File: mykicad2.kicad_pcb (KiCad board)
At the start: 2 copper layers, 11 parts, among them P1 CONN_01X06, Q1 MMBT3904, Q2 MMBT3906, Q3 IRF9540N

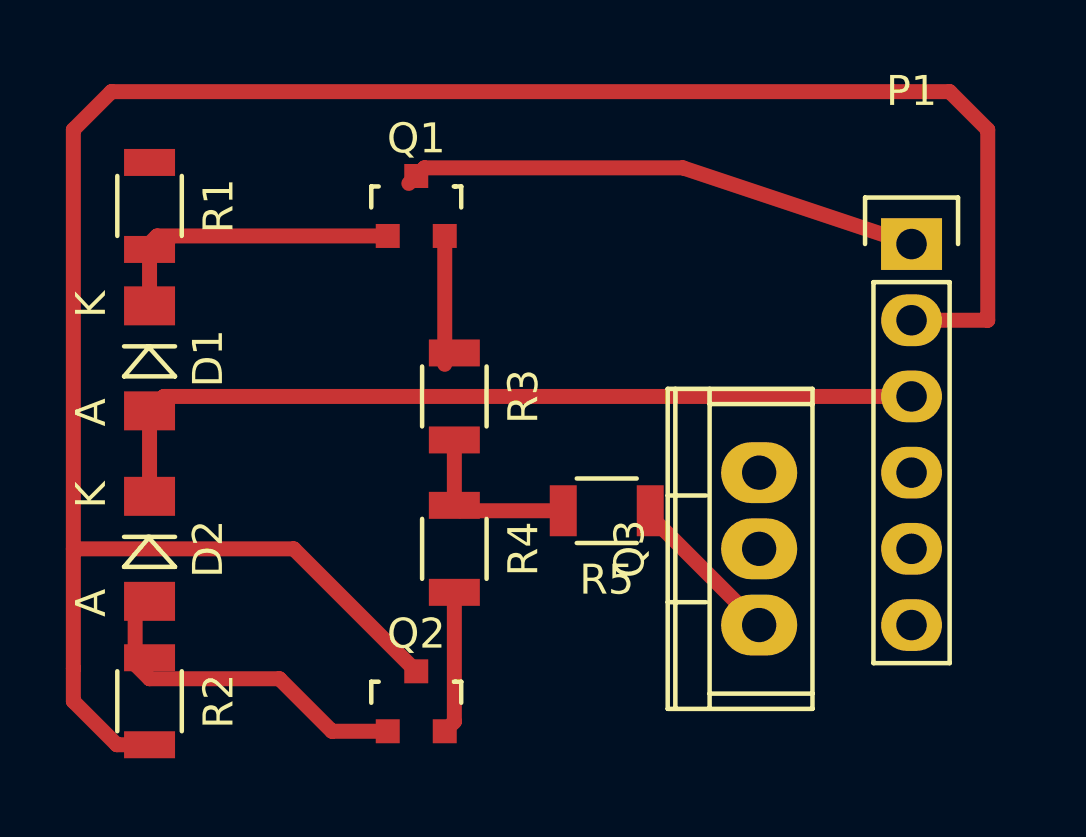
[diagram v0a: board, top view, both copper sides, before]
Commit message: add mosfet update traces
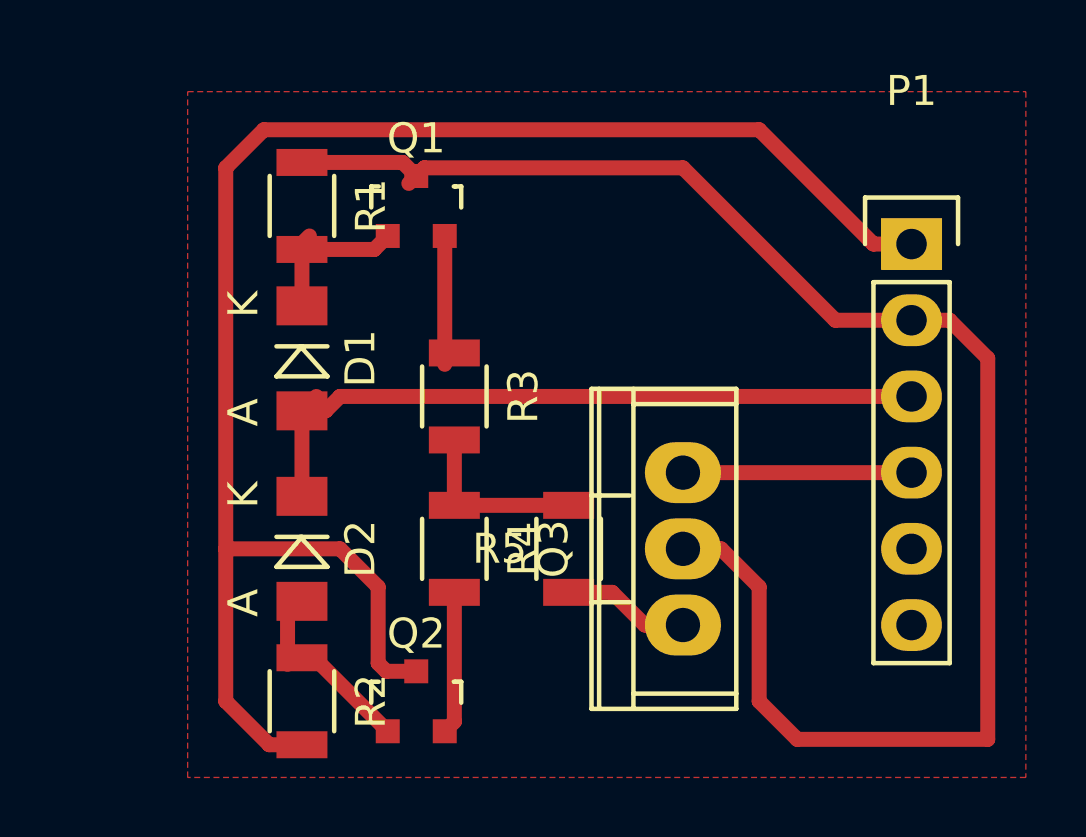
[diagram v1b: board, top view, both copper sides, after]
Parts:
- moved D1 5.08 mm to (154.9, 101.6)
- moved D2 5.08 mm to (154.9, 108.0)
- moved R1 5.08 mm to (154.9, 96.5)
- moved R2 5.08 mm to (154.9, 113.0)
- moved Q3 2.54 mm to (167.6, 108.0)
- moved R5 1.80 mm to (163.8, 108.0), turned to 90 degrees
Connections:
- P1 pad 1: VDD -> GND
- P1 pad 2: GND -> VDD
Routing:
- net VDD: track 17.4 -> 54.2 mm
- net GND: track 75.7 -> 55.4 mm
- net Net-(P1-Pad4): track 0.00 -> 7.62 mm
- net Net-(D2-Pad2): track 11.4 -> 5.98 mm
- net Net-(D1-Pad1): track 10.1 -> 5.48 mm
- net Net-(D1-Pad2): track 28.4 -> 24.0 mm
- net Net-(Q3-Pad1): track 5.31 -> 4.26 mm
- added copper zone on F.Cu, net GND
